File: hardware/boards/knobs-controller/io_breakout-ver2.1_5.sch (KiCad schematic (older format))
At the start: 15 parts, among them U3 ANALOG_DEVICES_AD7606BSTZANAL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

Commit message: 1.8 work-in-progress
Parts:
- C21, C22, C23, C24: footprint footprints:C0805K -> Capacitor_SMD:C_0805_2012Metric
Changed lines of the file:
@@
 F 0 "C21" H 3100 5745 59  0000 L BNN
 F 1 "0.1u" H 3070 5285 59  0000 L BNN
-F 2 "footprints:C0805K" H 3200 5600 50  0001 C CNN
+F 2 "Capacitor_SMD:C_0805_2012Metric" H 3200 5600 50  0001 C CNN
 F 3 "" H 3200 5600 50  0001 C CNN
 	1    3200 5600
@@
 F 0 "C22" H 3500 5845 59  0000 L BNN
 F 1 "0.1u" H 3470 5385 59  0000 L BNN
-F 2 "footprints:C0805K" H 3600 5700 50  0001 C CNN
+F 2 "Capacitor_SMD:C_0805_2012Metric" H 3600 5700 50  0001 C CNN
 F 3 "" H 3600 5700 50  0001 C CNN
 	1    3600 5700
@@
 F 0 "C23" H 3900 5945 59  0000 L BNN
 F 1 "0.1u" H 3870 5485 59  0000 L BNN
-F 2 "footprints:C0805K" H 4000 5800 50  0001 C CNN
+F 2 "Capacitor_SMD:C_0805_2012Metric" H 4000 5800 50  0001 C CNN
 F 3 "" H 4000 5800 50  0001 C CNN
 	1    4000 5800
@@
 F 0 "C24" H 4300 6045 59  0000 L BNN
 F 1 "0.1u" H 4270 5585 59  0000 L BNN
-F 2 "footprints:C0805K" H 4400 5900 50  0001 C CNN
+F 2 "Capacitor_SMD:C_0805_2012Metric" H 4400 5900 50  0001 C CNN
 F 3 "" H 4400 5900 50  0001 C CNN
 	1    4400 5900

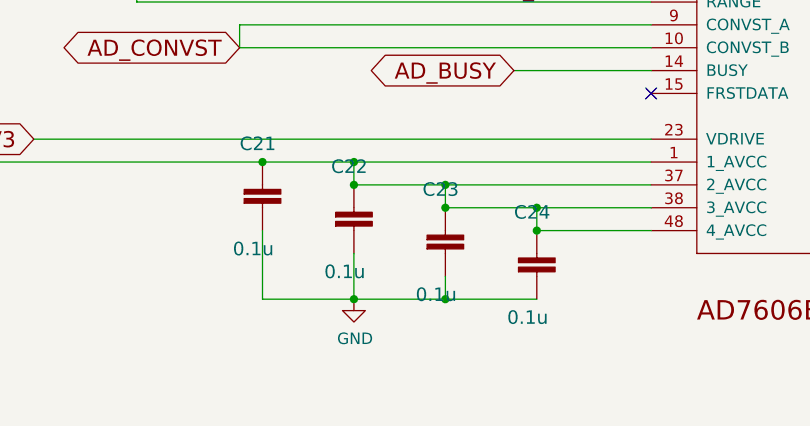
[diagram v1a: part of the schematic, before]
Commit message: 100nF changed to 0.1uF
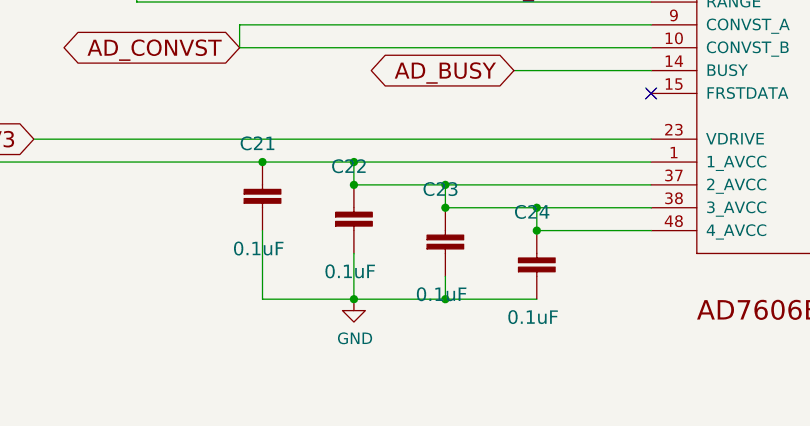
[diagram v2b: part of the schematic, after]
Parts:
- C21, C22, C23, C24: value 0.1u -> 0.1uF
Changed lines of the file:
@@
 AR Path="/5D7F4383/1D572C6C" Ref="C21"  Part="1"
 F 0 "C21" H 3100 5745 59  0000 L BNN
-F 1 "0.1u" H 3070 5285 59  0000 L BNN
+F 1 "0.1uF" H 3070 5285 59  0000 L BNN
 F 2 "Capacitor_SMD:C_0805_2012Metric" H 3200 5600 50  0001 C CNN
 F 3 "" H 3200 5600 50  0001 C CNN
@@
 AR Path="/5D7F4383/5C72CEA9" Ref="C22"  Part="1"
 F 0 "C22" H 3500 5845 59  0000 L BNN
-F 1 "0.1u" H 3470 5385 59  0000 L BNN
+F 1 "0.1uF" H 3470 5385 59  0000 L BNN
 F 2 "Capacitor_SMD:C_0805_2012Metric" H 3600 5700 50  0001 C CNN
 F 3 "" H 3600 5700 50  0001 C CNN
@@
 AR Path="/5D7F4383/742C1862" Ref="C23"  Part="1"
 F 0 "C23" H 3900 5945 59  0000 L BNN
-F 1 "0.1u" H 3870 5485 59  0000 L BNN
+F 1 "0.1uF" H 3870 5485 59  0000 L BNN
 F 2 "Capacitor_SMD:C_0805_2012Metric" H 4000 5800 50  0001 C CNN
 F 3 "" H 4000 5800 50  0001 C CNN
@@
 AR Path="/5D7F4383/D8AA1394" Ref="C24"  Part="1"
 F 0 "C24" H 4300 6045 59  0000 L BNN
-F 1 "0.1u" H 4270 5585 59  0000 L BNN
+F 1 "0.1uF" H 4270 5585 59  0000 L BNN
 F 2 "Capacitor_SMD:C_0805_2012Metric" H 4400 5900 50  0001 C CNN
 F 3 "" H 4400 5900 50  0001 C CNN

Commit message: changed c6 to 0805, updates to footprints to simplify BOM
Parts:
- C21, C22, C23, C24: symbol TopBreakout-eagle-import:C-EUC0805K -> knobs-eagle-import:C-EUC0805
- C26, C27: value 1.0uF -> 1uF; symbol TopBreakout-eagle-import:1.0UF-1206-50V-10% -> knobs-eagle-import:C-EUC0805
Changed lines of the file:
@@
 $EndComp
 $Comp
-L TopBreakout-eagle-import:C-EUC0805K C?
+L knobs-eagle-import:C-EUC0805 C?
 U 1 1 1D572C6C
 P 3200 5600
@@
 $EndComp
 $Comp
-L TopBreakout-eagle-import:C-EUC0805K C?
+L knobs-eagle-import:C-EUC0805 C?
 U 1 1 5C72CEA9
 P 3600 5700
@@
 $EndComp
 $Comp
-L TopBreakout-eagle-import:C-EUC0805K C?
+L knobs-eagle-import:C-EUC0805 C?
 U 1 1 742C1862
 P 4000 5800
@@
 $EndComp
 $Comp
-L TopBreakout-eagle-import:C-EUC0805K C?
+L knobs-eagle-import:C-EUC0805 C?
 U 1 1 D8AA1394
 P 4400 5900
@@
 $EndComp
 $Comp
-L TopBreakout-eagle-import:1.0UF-1206-50V-10% C?
+L knobs-eagle-import:C-EUC0805 C?
 U 1 1 B9947190
-P 9000 4200
+P 9000 4100
 AR Path="/B9947190" Ref="C?"  Part="1"
 AR Path="/5D7F4383/B9947190" Ref="C27"  Part="1"
-F 0 "C27" H 9060 4315 70  0000 L BNN
-F 1 "1.0uF" H 9060 4115 70  0000 L BNN
-F 2 "Capacitor_SMD:C_0805_2012Metric" H 9000 4200 50  0001 C CNN
-F 3 "" H 9000 4200 50  0001 C CNN
-	1    9000 4200
+F 0 "C27" H 9060 4215 70  0000 L BNN
+F 1 "1uF" H 9060 4015 70  0000 L BNN
+F 2 "Capacitor_SMD:C_0805_2012Metric" H 9000 4100 50  0001 C CNN
+F 3 "" H 9000 4100 50  0001 C CNN
+	1    9000 4100
 	1    0    0    -1
 $EndComp
 $Comp
-L TopBreakout-eagle-import:1.0UF-1206-50V-10% C?
+L knobs-eagle-import:C-EUC0805 C?
 U 1 1 ABE2F8F8
-P 8600 4300
+P 8600 4200
 AR Path="/ABE2F8F8" Ref="C?"  Part="1"
 AR Path="/5D7F4383/ABE2F8F8" Ref="C26"  Part="1"
-F 0 "C26" H 8660 4415 70  0000 L BNN
-F 1 "1.0uF" H 8660 4215 70  0000 L BNN
-F 2 "Capacitor_SMD:C_0805_2012Metric" H 8600 4300 50  0001 C CNN
-F 3 "" H 8600 4300 50  0001 C CNN
-	1    8600 4300
+F 0 "C26" H 8660 4315 70  0000 L BNN
+F 1 "1uF" H 8660 4115 70  0000 L BNN
+F 2 "Capacitor_SMD:C_0805_2012Metric" H 8600 4200 50  0001 C CNN
+F 3 "" H 8600 4200 50  0001 C CNN
+	1    8600 4200
 	1    0    0    -1
 $EndComp
